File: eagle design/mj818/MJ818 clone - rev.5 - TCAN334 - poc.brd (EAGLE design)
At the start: 35 x 35 mm, 38 parts, among them IC202 LDK320AM33R, IC302 STM32F042G6U6, IC401 TCAN334, IC506 MAX16820, IC507 SQA470EEJ-T1_GE3, IC601 MAX16839, J1 CAN, J2 Power Supply, J3 LED

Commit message: MJ818: confirmed pulldown resistor for rear LED PWM line (driver input side) is needed
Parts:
- removed R102: 10k, rcl:R0402
- added R601: 10k, rcl:R0402
- renumbered J1 to J103, J2 to J101, J3 to J102
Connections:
- net DIM_REAR: now also R601.2; no longer R102.2
- net GND: now also R601.1; no longer R102.1
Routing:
- net GND: track 4.19 -> 3.86 mm, vias 52 -> 51

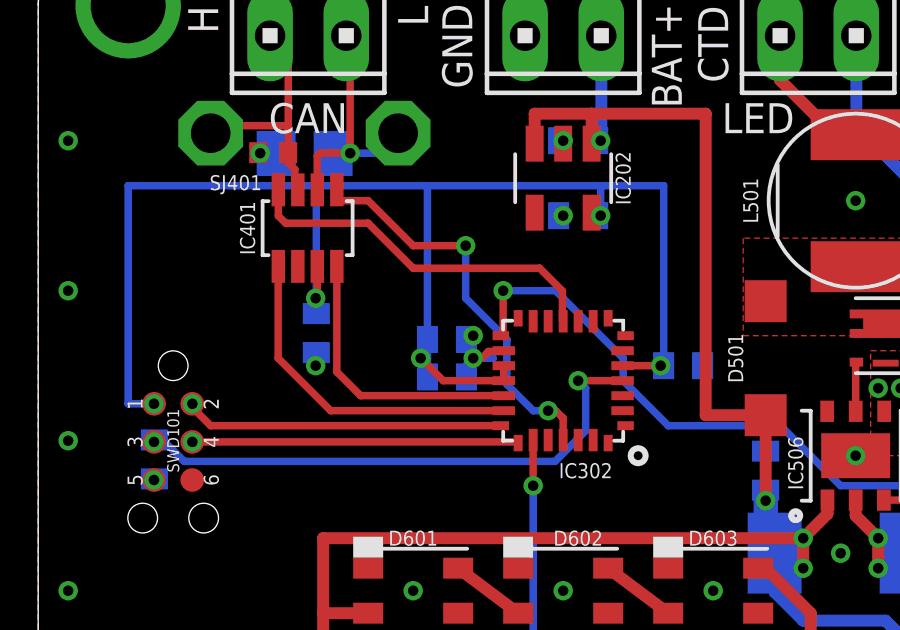
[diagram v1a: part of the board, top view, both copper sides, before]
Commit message: board revision 5a: - removed CAN infra shutdown pin, since it is not needed
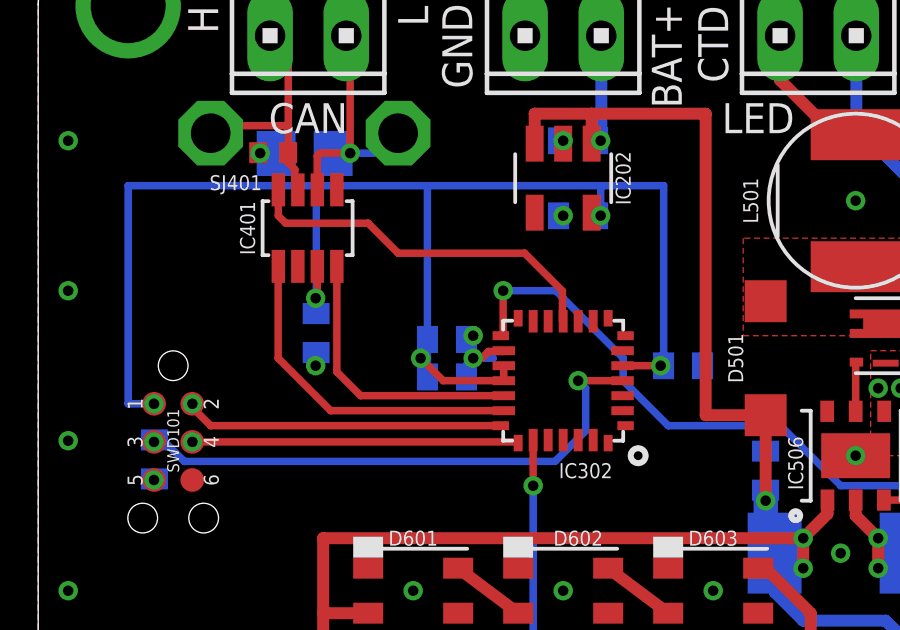
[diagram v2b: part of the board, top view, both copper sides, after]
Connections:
- removed net !SHDN!: IC302.25_PB4, IC401.P$5
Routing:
- net !SHDN!: track 13.5 -> 0.00 mm, vias 2 -> 0
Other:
- board text added: "MJ818 POC ejovrh rev.5a"
- board text removed: "MJ818 POC ejovrh rev.5"
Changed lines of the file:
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@@
 <grid distance="0.25" unitdist="mm" unit="mm" style="dots" multiple="1" display="yes" altdistance="0.125" altunitdist="mm" altunit="mm"/>
 <layers>
-<layer number="1" name="Top" color="4" fill="1" visible="no" active="yes"/>
+<layer number="1" name="Top" color="4" fill="1" visible="yes" active="yes"/>
 <layer number="2" name="Route2" color="16" fill="1" visible="no" active="no"/>
 <layer number="3" name="Route3" color="17" fill="1" visible="no" active="no"/>
@@
 <layer number="14" name="Route14" color="22" fill="1" visible="no" active="no"/>
 <layer number="15" name="Route15" color="23" fill="1" visible="no" active="no"/>
-<layer number="16" name="Bottom" color="1" fill="1" visible="yes" active="yes"/>
+<layer number="16" name="Bottom" color="1" fill="1" visible="no" active="yes"/>
 <layer number="17" name="Pads" color="2" fill="1" visible="yes" active="yes"/>
 <layer number="18" name="Vias" color="2" fill="1" visible="yes" active="yes"/>
 <layer number="19" name="Unrouted" color="6" fill="1" visible="yes" active="yes"/>
 <layer number="20" name="Dimension" color="24" fill="1" visible="yes" active="yes"/>
-<layer number="21" name="tPlace" color="7" fill="1" visible="no" active="yes"/>
-<layer number="22" name="bPlace" color="7" fill="1" visible="yes" active="yes"/>
-<layer number="23" name="tOrigins" color="15" fill="1" visible="no" active="yes"/>
-<layer number="24" name="bOrigins" color="15" fill="1" visible="yes" active="yes"/>
-<layer number="25" name="tNames" color="7" fill="1" visible="no" active="yes"/>
-<layer number="26" name="bNames" color="7" fill="1" visible="yes" active="yes"/>
+<layer number="21" name="tPlace" color="7" fill="1" visible="yes" active="yes"/>
+<layer number="22" name="bPlace" color="7" fill="1" visible="no" active="yes"/>
+<layer number="23" name="tOrigins" color="15" fill="1" visible="yes" active="yes"/>
+<layer number="24" name="bOrigins" color="15" fill="1" visible="no" active="yes"/>
+<layer number="25" name="tNames" color="7" fill="1" visible="yes" active="yes"/>
+<layer number="26" name="bNames" color="7" fill="1" visible="no" active="yes"/>
 <layer number="27" name="tValues" color="7" fill="1" visible="no" active="yes"/>
 <layer number="28" name="bValues" color="7" fill="1" visible="no" active="yes"/>
-<layer number="29" name="tStop" color="7" fill="3" visible="no" active="yes"/>
-<layer number="30" name="bStop" color="7" fill="6" visible="yes" active="yes"/>
+<layer number="29" name="tStop" color="7" fill="3" visible="yes" active="yes"/>
+<layer number="30" name="bStop" color="7" fill="6" visible="no" active="yes"/>
 <layer number="31" name="tCream" color="7" fill="4" visible="no" active="yes"/>
 <layer number="32" name="bCream" color="7" fill="5" visible="no" active="yes"/>
@@
 <layer number="37" name="tTest" color="7" fill="1" visible="no" active="yes"/>
 <layer number="38" name="bTest" color="7" fill="1" visible="no" active="yes"/>
-<layer number="39" name="tKeepout" color="4" fill="11" visible="no" active="yes"/>
-<layer number="40" name="bKeepout" color="1" fill="11" visible="yes" active="yes"/>
-<layer number="41" name="tRestrict" color="4" fill="10" visible="no" active="yes"/>
-<layer number="42" name="bRestrict" color="1" fill="10" visible="yes" active="yes"/>
+<layer number="39" name="tKeepout" color="4" fill="11" visible="yes" active="yes"/>
+<layer number="40" name="bKeepout" color="1" fill="11" visible="no" active="yes"/>
+<layer number="41" name="tRestrict" color="4" fill="10" visible="yes" active="yes"/>
+<layer number="42" name="bRestrict" color="1" fill="10" visible="no" active="yes"/>
 <layer number="43" name="vRestrict" color="2" fill="10" visible="yes" active="yes"/>
 <layer number="44" name="Drills" color="7" fill="1" visible="no" active="yes"/>
@@
 <layer number="49" name="Reference" color="7" fill="1" visible="no" active="yes"/>
 <layer number="50" name="dxf" color="7" fill="1" visible="no" active="no"/>
-<layer number="51" name="tDocu" color="7" fill="1" visible="no" active="yes"/>
-<layer number="52" name="bDocu" color="7" fill="1" visible="yes" active="yes"/>
+<layer number="51" name="tDocu" color="7" fill="1" visible="yes" active="yes"/>
+<layer number="52" name="bDocu" color="7" fill="1" visible="no" active="yes"/>
 <layer number="53" name="tGND_GNDA" color="7" fill="9" visible="no" active="no"/>
 <layer number="54" name="bGND_GNDA" color="1" fill="9" visible="no" active="no"/>
@@
 <wire x1="3" y1="3" x2="3" y2="32" width="0.1524" layer="49"/>
 <text x="4" y="9.5" locked="yes" size="1" layer="29" font="vector" ratio="12" rot="R270" align="center">MJ818 POC
-ejovrh rev.5</text>
+ejovrh rev.5a</text>
 <wire x1="34" y1="32" x2="34" y2="3" width="2" layer="29" locked="yes"/>
 <wire x1="34" y1="3" x2="32" y2="1" width="2" layer="29" curve="-90" locked="yes"/>
@@
 <wire x1="8.005" y1="24.995" x2="8.25" y2="24.75" width="0.25" layer="1"/>
 <wire x1="8.25" y1="24.75" x2="11" y2="24.75" width="0.25" layer="1"/>
-<wire x1="11" y1="24.75" x2="12.5" y2="23.25" width="0.25" layer="1"/>
+<wire x1="11" y1="24.75" x2="12" y2="23.75" width="0.25" layer="1"/>
 <wire x1="17.475" y1="22.48961875" x2="17.475" y2="21.505" width="0.25" layer="1"/>
 <wire x1="17.475" y1="21.505" x2="17.5" y2="21.48" width="0.25" layer="1"/>
-<wire x1="16.71461875" y1="23.25" x2="17.475" y2="22.48961875" width="0.25" layer="1"/>
-<wire x1="12.5" y1="23.25" x2="16.71461875" y2="23.25" width="0.25" layer="1"/>
-</signal>
-<signal name="!SHDN!">
-<contactref element="IC302" pad="25_PB4"/>
-<contactref element="IC401" pad="P$5"/>
-<via x="17" y="18.5" extent="1-16" drill="0.35"/>
-<wire x1="17" y1="18.5" x2="17.25" y2="18.5" width="0.25" layer="1"/>
-<wire x1="17.5" y1="18.25" x2="17.25" y2="18.5" width="0.25" layer="1"/>
-<wire x1="17.5" y1="18.25" x2="17.5" y2="17.52" width="0.25" layer="1"/>
-<wire x1="11" y1="25.5" x2="10.065" y2="25.5" width="0.25" layer="1"/>
-<wire x1="10.065" y1="25.5" x2="9.955" y2="25.61" width="0.25" layer="1"/>
-<wire x1="9.955" y1="25.61" x2="9.955" y2="25.86" width="0.25" layer="1"/>
-<via x="14.25" y="24" extent="1-16" drill="0.35"/>
-<wire x1="14.25" y1="24" x2="12.5" y2="24" width="0.25" layer="1"/>
-<wire x1="12.5" y1="24" x2="11" y2="25.5" width="0.25" layer="1"/>
-<wire x1="14.25" y1="24" x2="14.25" y2="22.25" width="0.25" layer="16"/>
-<wire x1="15.625" y1="20.875" x2="14.25" y2="22.25" width="0.25" layer="16"/>
-<wire x1="17" y1="18.5" x2="16.5" y2="18.5" width="0.25" layer="16"/>
-<wire x1="16.5" y1="18.5" x2="15.625" y2="19.375" width="0.25" layer="16"/>
-<wire x1="15.625" y1="19.375" x2="15.625" y2="20.875" width="0.25" layer="16"/>
+<wire x1="16.21461875" y1="23.75" x2="17.475" y2="22.48961875" width="0.25" layer="1"/>
+<wire x1="12" y1="23.75" x2="16.21461875" y2="23.75" width="0.25" layer="1"/>
 </signal>
 <signal name="CAN_INFRA:CAN_JMPR" class="3">

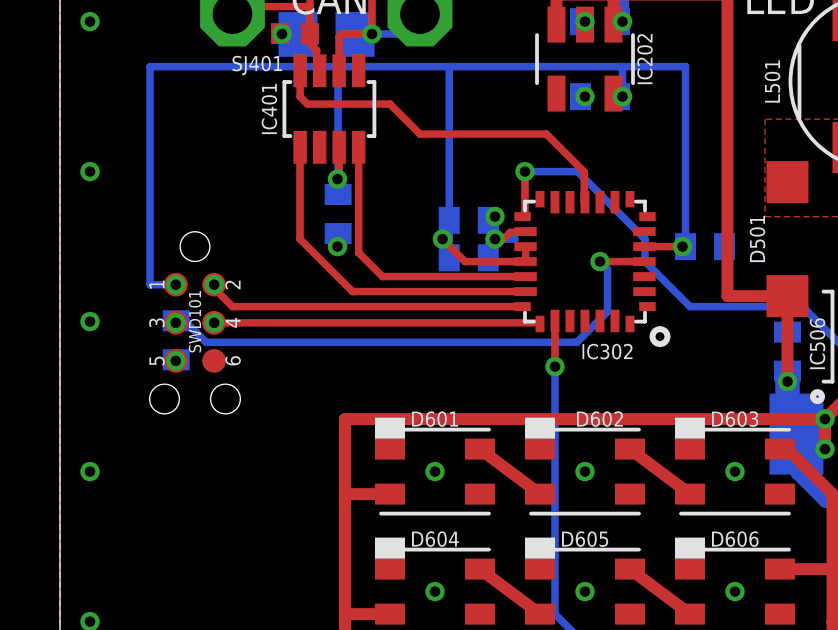
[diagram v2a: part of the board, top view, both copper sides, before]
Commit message: - sized TAG connect vias up to 0.45mm
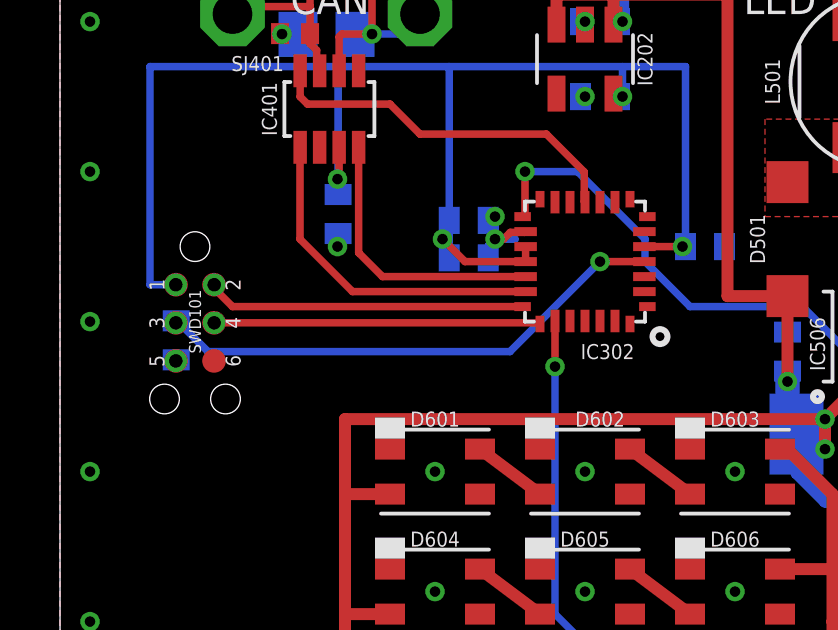
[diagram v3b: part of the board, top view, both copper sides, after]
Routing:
- net SYS_NRST: track 18.4 -> 17.4 mm
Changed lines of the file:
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@@
 <via x="32" y="3" extent="1-16" drill="2.5" locked="yes"/>
 <via x="3" y="3" extent="1-16" drill="2.5" locked="yes"/>
-<via x="3.86" y="16.19" extent="1-16" drill="0.35"/>
+<via x="3.86" y="16.19" extent="1-16" drill="0.45"/>
 <via x="17.5" y="25" extent="1-16" drill="0.35"/>
 <via x="28.75" y="8.5" extent="1-16" drill="0.35"/>
@@
 <contactref element="C405" pad="1"/>
 <contactref element="IC401" pad="P$3"/>
-<via x="3.86" y="18.73" extent="1-16" drill="0.35"/>
+<via x="3.86" y="18.73" extent="1-16" drill="0.45"/>
 <via x="18.75" y="25" extent="1-16" drill="0.35"/>
 <via x="9.25" y="22.25" extent="1-16" drill="0.35"/>
@@
 <contactref element="SWD101" pad="2_T_SWDIO"/>
 <contactref element="IC302" pad="21_PA13"/>
-<via x="5.14" y="18.73" extent="1-16" drill="0.35"/>
+<via x="5.14" y="18.73" extent="1-16" drill="0.45"/>
 <wire x1="15.42" y1="18" x2="5.75" y2="18" width="0.25" layer="1"/>
 <wire x1="5.75" y1="18" x2="5.14" y2="18.61" width="0.25" layer="1"/>
@@
 <contactref element="IC302" pad="4_NRST"/>
 <contactref element="C307" pad="2"/>
-<via x="3.86" y="17.46" extent="1-16" drill="0.35"/>
+<via x="3.86" y="17.46" extent="1-16" drill="0.45"/>
 <wire x1="3.865" y1="17.46" x2="3.86" y2="17.46" width="0.25" layer="1"/>
 <wire x1="3.875" y1="17.525" x2="3.86" y2="17.525" width="0.25" layer="16"/>
@@
 <wire x1="19.48" y1="19.5" x2="18" y2="19.5" width="0.25" layer="1"/>
 <via x="18" y="19.5" extent="1-16" drill="0.35"/>
-<wire x1="4.15575625" y1="17.525" x2="3.875" y2="17.525" width="0.25" layer="16"/>
-<wire x1="4.87075625" y1="16.81" x2="4.15575625" y2="17.525" width="0.25" layer="16"/>
-<wire x1="17.22924375" y1="16.81" x2="4.87075625" y2="16.81" width="0.25" layer="16"/>
-<wire x1="18" y1="19.5" x2="18.25" y2="19.25" width="0.25" layer="16"/>
-<wire x1="18.25" y1="19.25" x2="18.25" y2="17.83075625" width="0.25" layer="16"/>
-<wire x1="18.25" y1="17.83075625" x2="17.22924375" y2="16.81" width="0.25" layer="16"/>
+<wire x1="3.90575625" y1="17.525" x2="3.875" y2="17.525" width="0.25" layer="16"/>
+<wire x1="4.93075625" y1="16.5" x2="3.90575625" y2="17.525" width="0.25" layer="16"/>
+<wire x1="15" y1="16.5" x2="4.93075625" y2="16.5" width="0.25" layer="16"/>
+<wire x1="18" y1="19.5" x2="15" y2="16.5" width="0.25" layer="16"/>
 </signal>
 <signal name="SYS_SWCLK" class="3">
 <contactref element="SWD101" pad="4_T_SWCLK"/>
 <contactref element="IC302" pad="22_PA14"/>
-<via x="5.14" y="17.46" extent="1-16" drill="0.35"/>
+<via x="5.14" y="17.46" extent="1-16" drill="0.45"/>
 <wire x1="5.135" y1="17.46" x2="5.14" y2="17.46" width="0.25" layer="1"/>
 <wire x1="5.135" y1="17.46" x2="16" y2="17.46" width="0.25" layer="1"/>

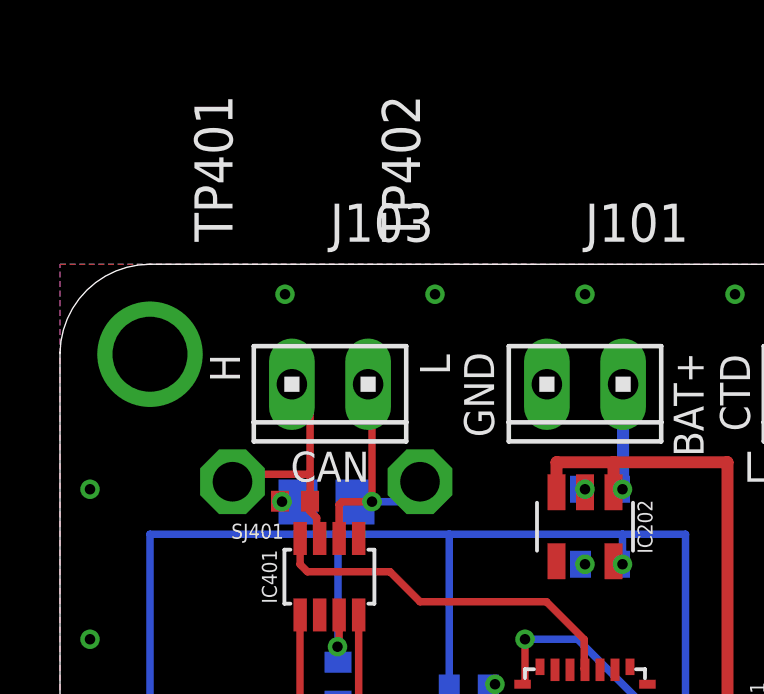
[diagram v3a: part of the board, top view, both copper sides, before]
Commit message: - removed CAN test points, since they are useless
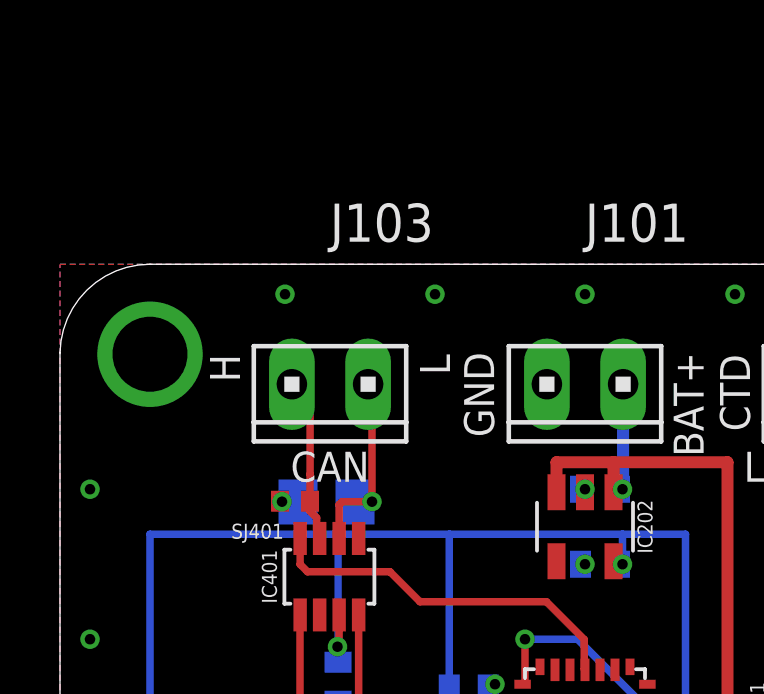
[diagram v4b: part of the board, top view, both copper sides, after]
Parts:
- removed TP401, TP402: PTR1PAD1-13, testpad:P1-13
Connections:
- net CAN_H: no longer TP401.TP
- net CAN_L: no longer TP402.TP
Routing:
- net CAN_H: track 8.21 -> 5.52 mm
- net CAN_L: track 8.68 -> 6.81 mm
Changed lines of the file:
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@@
 <attribute name="VALUE" x="4.5" y="20" locked="yes" size="0.5" layer="27" font="vector" align="center"/>
-</element>
-<element name="TP401" library="testpad" library_urn="urn:adsk.eagle:library:385" package="P1-13" package3d_urn="urn:adsk.eagle:package:27946/1" value="PTR1PAD1-13" x="5.75" y="27.75" locked="yes" smashed="yes">
-<attribute name="NAME" x="5.75" y="35.75" locked="yes" size="1.27" layer="25" ratio="10" rot="R90"/>
-<attribute name="POPULARITY" value="2" x="6.25" y="27.75" locked="yes" size="1.778" layer="27" display="off"/>
-<attribute name="TP_SIGNAL_NAME" value="" x="4.48" y="25.21" locked="yes" size="1" layer="37"/>
-<attribute name="VALUE" x="5.75" y="27.75" locked="yes" size="0.0254" layer="27"/>
-</element>
-<element name="TP402" library="testpad" library_urn="urn:adsk.eagle:library:385" package="P1-13" package3d_urn="urn:adsk.eagle:package:27946/1" value="PTR1PAD1-13" x="12" y="27.75" locked="yes" smashed="yes">
-<attribute name="NAME" x="12" y="35.75" locked="yes" size="1.27" layer="25" ratio="10" rot="R90"/>
-<attribute name="POPULARITY" value="2" x="12.5" y="27.75" locked="yes" size="1.778" layer="27" display="off"/>
-<attribute name="TP_SIGNAL_NAME" value="" x="10.73" y="25.21" locked="yes" size="1" layer="37"/>
-<attribute name="VALUE" x="12" y="27.75" locked="yes" size="0.0254" layer="27"/>
 </element>
 <element name="J101" library="con-amp" library_urn="urn:adsk.eagle:library:127" package="10X02MTA" package3d_urn="urn:adsk.eagle:package:8081649/1" value="Power Supply" x="17.5" y="31" locked="yes" smashed="yes" rot="R180">
@@
 <wire x1="8.335" y1="26.76461875" x2="8.335" y2="27.1" width="0.25" layer="1"/>
 <wire x1="8.555" y1="26.54461875" x2="8.335" y2="26.76461875" width="0.25" layer="1"/>
-<contactref element="TP401" pad="TP"/>
 <contactref element="J103" pad="1"/>
 <wire x1="7.73" y1="31" x2="8.335" y2="30.395" width="0.25" layer="1"/>
 <wire x1="8.335" y1="30.395" x2="8.335" y2="28" width="0.25" layer="1"/>
 <wire x1="8.335" y1="28" x2="8.335" y2="27.1" width="0.25" layer="1"/>
-<wire x1="5.75" y1="27.75" x2="6" y2="28" width="0.25" layer="1"/>
-<wire x1="6" y1="28" x2="8.335" y2="28" width="0.25" layer="1"/>
 </signal>
 <signal name="CAN_L" class="3">
@@
 <wire x1="9.835" y1="27.075" x2="9.835" y2="27.085" width="0.25" layer="16"/>
 <wire x1="9.835" y1="27.085" x2="10.4" y2="27.085" width="0.25" layer="16"/>
-<contactref element="TP402" pad="TP"/>
 <contactref element="J103" pad="2"/>
 <wire x1="10.27" y1="31" x2="10.4" y2="30.87" width="0.25" layer="1"/>
 <wire x1="10.4" y1="30.87" x2="10.4" y2="27.085" width="0.25" layer="1"/>
-<wire x1="10.4" y1="27.085" x2="11.335" y2="27.085" width="0.25" layer="16"/>
-<wire x1="11.335" y1="27.085" x2="12" y2="27.75" width="0.25" layer="16"/>
 </signal>
 <signal name="3V3" class="4">
